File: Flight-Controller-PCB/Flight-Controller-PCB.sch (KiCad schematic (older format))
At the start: 24 parts, among them J1 Power_In, J2 ESC_1, J3 ESC_2, J4 ESC_3, J5 ESC_4, J6 Receiver, J7 Aux, U1 MCP6001U

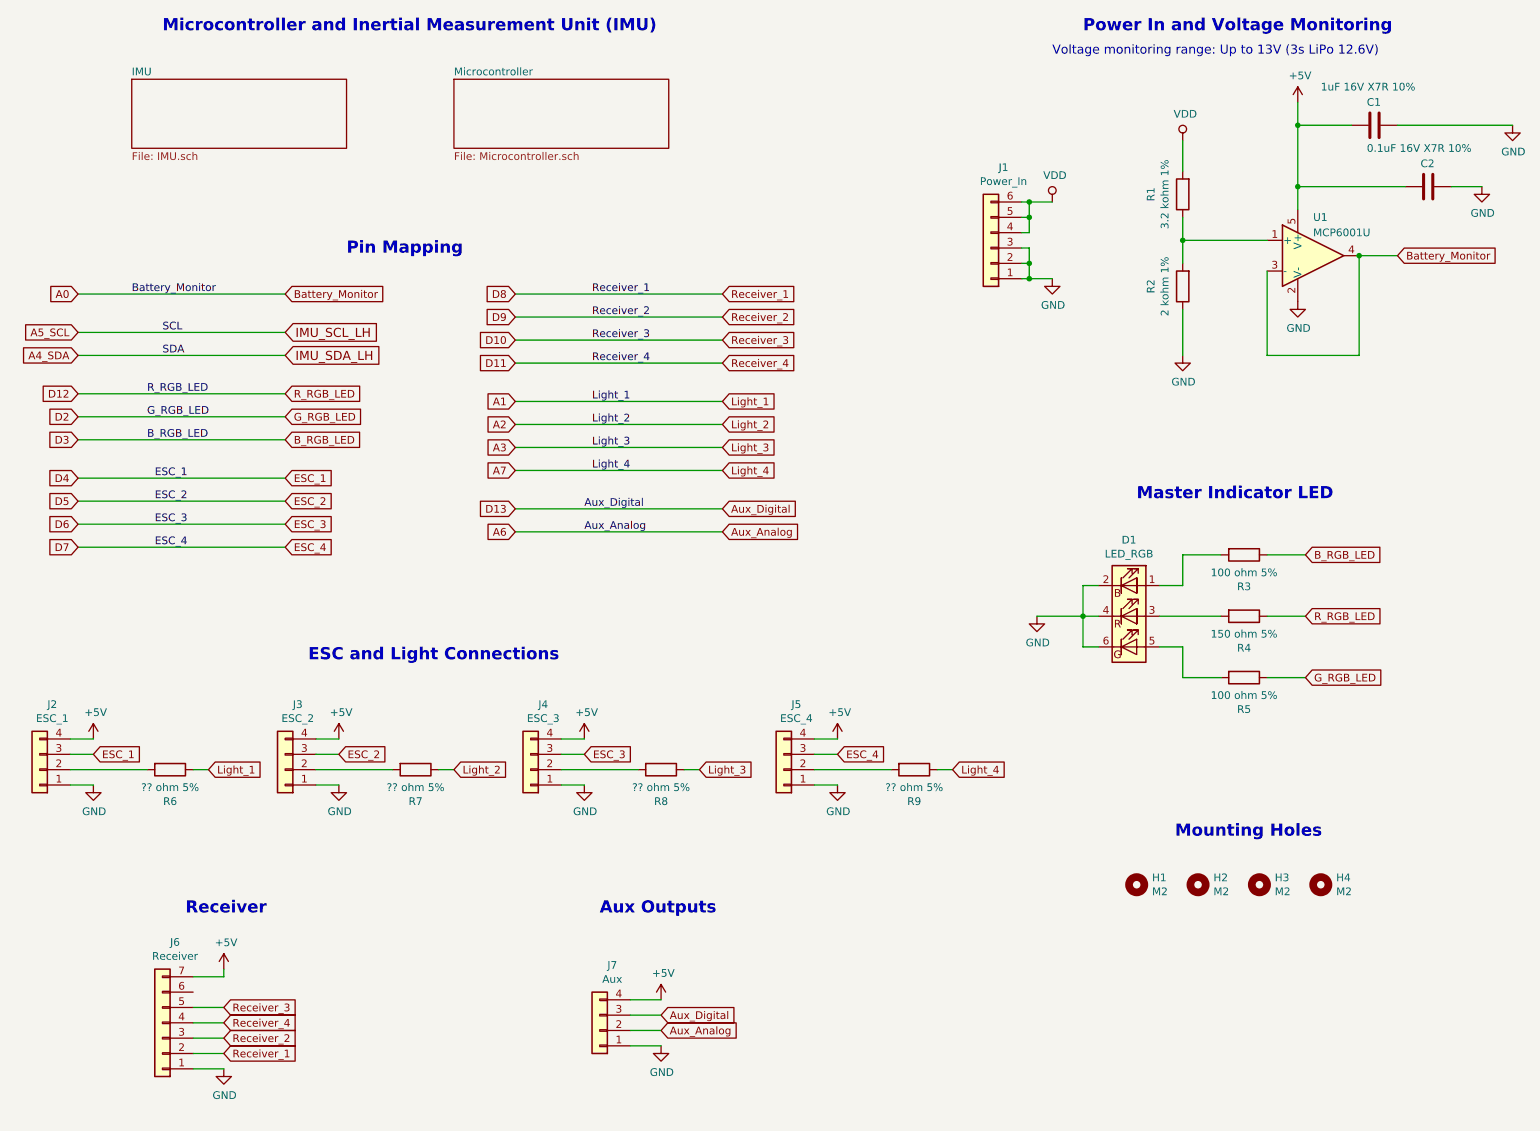
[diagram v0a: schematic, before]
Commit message: Deleted majority of unused components. Started schematic for new MCU
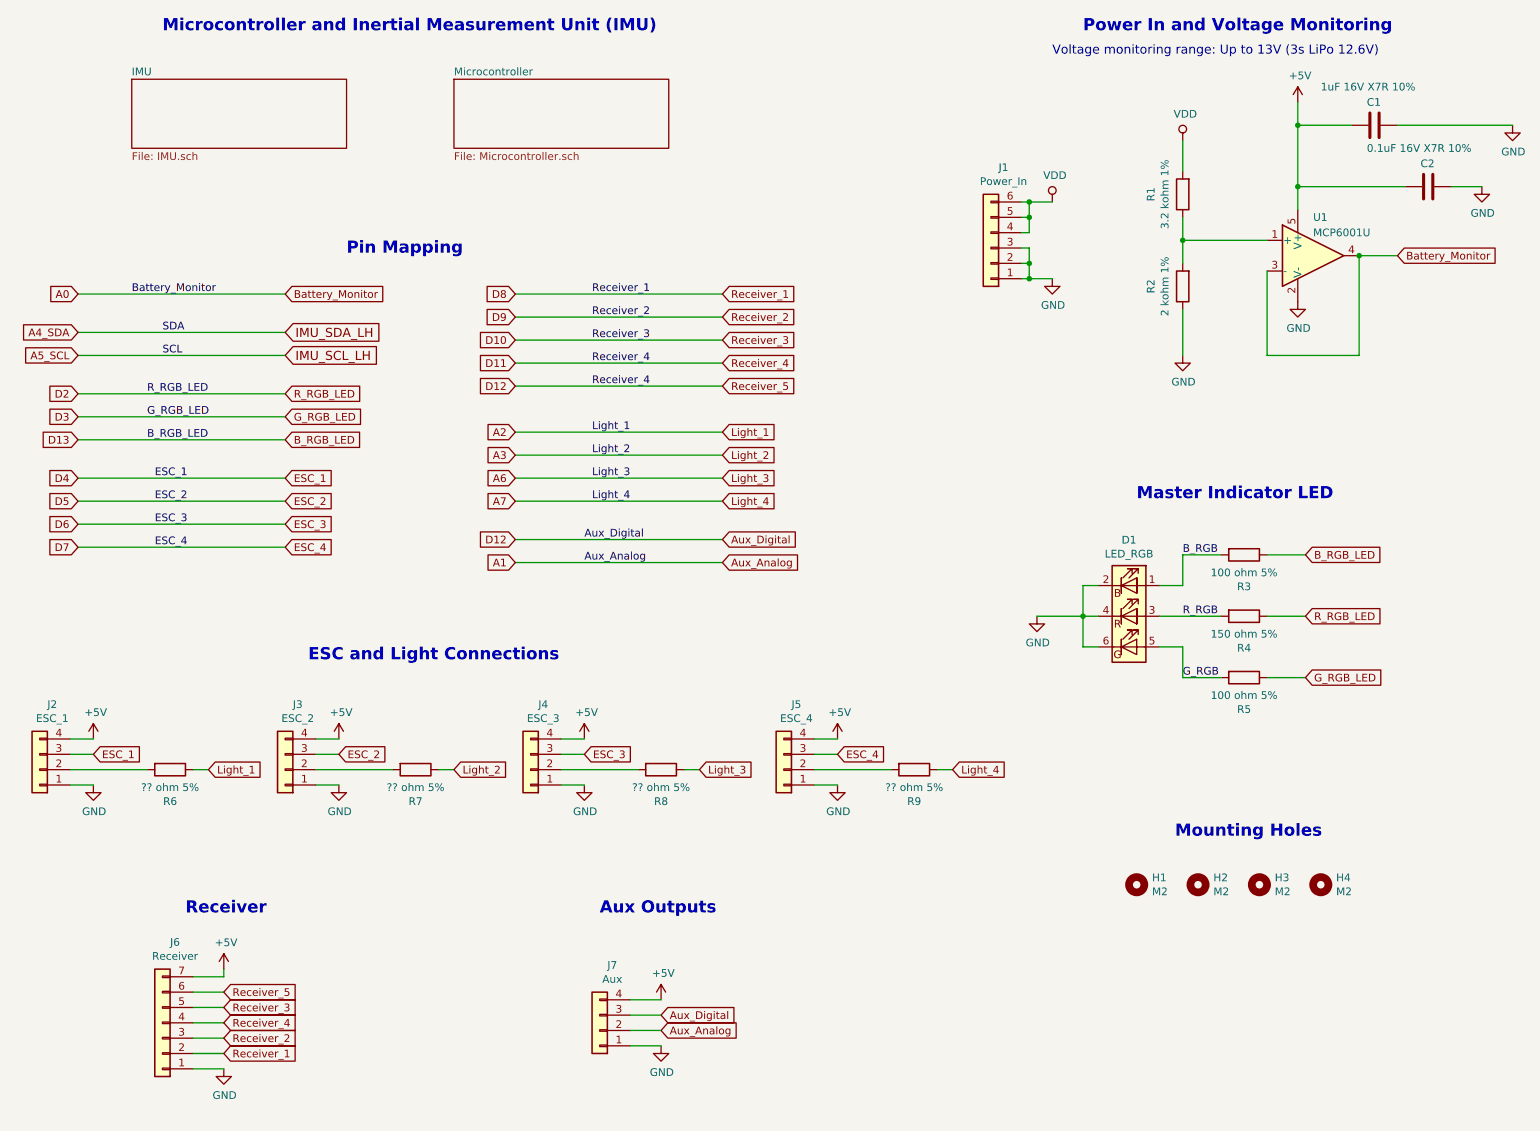
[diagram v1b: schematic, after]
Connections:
- net D11 is gone; now on net Aux_Digital: J6.4 (Pin_4)
- net D12 is gone; now on net D2: R4.1
- net A1: now also J7.2 (Pin_2); no longer R6.1
- net A2: now also R6.1; no longer R7.1
- net A3: now also R7.1; no longer R8.1
- net A6: now also R8.1; no longer J7.2 (Pin_2)
- net Aux_Digital: now also J6.6 (Pin_6)
- net D2: no longer R5.1
- net B_RGB: now reaches D1.1 (RA), R3.2
- net R_RGB: now reaches D1.3 (GA), R4.2
- net G_RGB: now reaches D1.5 (BA), R5.2
- new net D3: R5.1
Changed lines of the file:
@@
 EESchema Schematic File Version 4
-LIBS:Main-Board-cache
 EELAYER 30 0
 EELAYER END
@@
 	9350 2200 9600 2200
 Connection ~ 9350 2200
+Text GLabel 2350 2850 2    59   Input ~ 0
+IMU_SCL_LH
 Text GLabel 2350 2700 2    59   Input ~ 0
-IMU_SCL_LH
-Text GLabel 2350 2850 2    59   Input ~ 0
 IMU_SDA_LH
+Text GLabel 1000 2850 0    50   Input ~ 0
+A5_SCL
 Text GLabel 1000 2700 0    50   Input ~ 0
-A5_SCL
-Text GLabel 1000 2850 0    50   Input ~ 0
 A4_SDA
 Text Notes 7900 3800 0    79   ~ 16
@@
 	5200 2900 3850 2900
 Text GLabel 1000 3250 0    50   Input ~ 0
-D2
+D3
 Wire Wire Line
 	1000 3100 2350 3100
@@
 	2350 3400 1000 3400
 Wire Wire Line
+	1000 2850 2350 2850
+Wire Wire Line
 	1000 2700 2350 2700
 Wire Wire Line
-	1000 2850 2350 2850
-Wire Wire Line
 	1000 2450 2350 2450
-Text GLabel 5200 3150 2    50   Input ~ 0
+Text GLabel 5200 3350 2    50   Input ~ 0
 Light_1
-Text GLabel 5200 3300 2    50   Input ~ 0
+Text GLabel 5200 3500 2    50   Input ~ 0
 Light_2
-Text GLabel 5200 3450 2    50   Input ~ 0
+Text GLabel 5200 3650 2    50   Input ~ 0
 Light_3
-Text GLabel 5200 3600 2    50   Input ~ 0
+Text GLabel 5200 3800 2    50   Input ~ 0
 Light_4
-Text GLabel 3850 3150 0    50   Input ~ 0
-A1
-Text GLabel 3850 3300 0    50   Input ~ 0
+Text GLabel 3850 3350 0    50   Input ~ 0
 A2
-Text GLabel 3850 3450 0    50   Input ~ 0
+Text GLabel 3850 3500 0    50   Input ~ 0
 A3
-Text GLabel 3850 3600 0    50   Input ~ 0
+Text GLabel 3850 3650 0    50   Input ~ 0
+A6
+Text GLabel 3850 3800 0    50   Input ~ 0
 A7
 Wire Wire Line
-	3850 3150 5200 3150
-Wire Wire Line
-	5200 3300 3850 3300
-Wire Wire Line
-	3850 3450 5200 3450
-Wire Wire Line
-	5200 3600 3850 3600
+	3850 3350 5200 3350
+Wire Wire Line
+	5200 3500 3850 3500
+Wire Wire Line
+	3850 3650 5200 3650
+Wire Wire Line
+	5200 3800 3850 3800
 Text GLabel 1850 5550 2    50   Input ~ 0
 Light_1
@@
 Text Label 1350 2450 0    50   ~ 0
 Battery_Monitor
+Text Label 1550 2850 0    50   ~ 0
+SCL
 Text Label 1550 2700 0    50   ~ 0
-SCL
-Text Label 1550 2850 0    50   ~ 0
 SDA
 Text Label 1450 3100 0    50   ~ 0
@@
 $EndComp
 Text GLabel 1000 3100 0    50   Input ~ 0
-D12
+D2
 Text GLabel 1000 3400 0    50   Input ~ 0
-D3
+D13
 Text Label 4350 2450 0    50   ~ 0
 Receiver_1
@@
 Text Label 4350 2900 0    50   ~ 0
 Receiver_4
-Text Label 4350 3150 0    50   ~ 0
+Text Label 4350 3350 0    50   ~ 0
 Light_1
-Text Label 4350 3300 0    50   ~ 0
+Text Label 4350 3500 0    50   ~ 0
 Light_2
-Text Label 4350 3450 0    50   ~ 0
+Text Label 4350 3650 0    50   ~ 0
 Light_3
-Text Label 4350 3600 0    50   ~ 0
+Text Label 4350 3800 0    50   ~ 0
 Light_4
 Wire Wire Line
@@
 Text Notes 4400 6500 0    79   ~ 16
 Aux Outputs
-Text GLabel 3850 3850 0    50   Input ~ 0
-D13
-Text GLabel 3850 4000 0    50   Input ~ 0
-A6
-Text GLabel 5200 3850 2    50   Input ~ 0
+Text GLabel 3850 4050 0    50   Input ~ 0
+D12
+Text GLabel 3850 4200 0    50   Input ~ 0
+A1
+Text GLabel 5200 4050 2    50   Input ~ 0
 Aux_Digital
-Text GLabel 5200 4000 2    50   Input ~ 0
+Text GLabel 5200 4200 2    50   Input ~ 0
 Aux_Analog
 Wire Wire Line
-	3850 3850 5200 3850
-Wire Wire Line
-	5200 4000 3850 4000
-Text Label 4300 3850 0    50   ~ 0
+	3850 4050 5200 4050
+Wire Wire Line
+	5200 4200 3850 4200
+Text Label 4300 4050 0    50   ~ 0
 Aux_Digital
-Text Label 4300 4000 0    50   ~ 0
+Text Label 4300 4200 0    50   ~ 0
 Aux_Analog
 Text GLabel 4800 7150 2    50   Input ~ 0
@@
 Wire Wire Line
 	8750 4550 9000 4550
+Text GLabel 5200 3050 2    50   Input ~ 0
+Receiver_5
+Text GLabel 3850 3050 0    50   Input ~ 0
+D12
+Wire Wire Line
+	5200 3050 3850 3050
+Text Label 4350 3050 0    50   ~ 0
+Receiver_4
+Text GLabel 1950 7000 2    50   Input ~ 0
+Receiver_5
+Wire Wire Line
+	1750 7000 1950 7000
+Text Label 8200 4150 0    50   ~ 0
+B_RGB
+Text Label 8200 4550 0    50   ~ 0
+R_RGB
+Text Label 8200 4950 0    50   ~ 0
+G_RGB
 $EndSCHEMATC

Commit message: Push before branch switch
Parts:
- added D? (x2): LED, LED_SMD:LED_0603_1608Metric_Pad1.05x0.95mm_HandSolder, symbol Device:LED
- added R? (x2): ?? ohm 5%, Resistor_SMD:R_0603_1608Metric_Pad1.05x0.95mm_HandSolder, symbol Device:R
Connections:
- net +5V: now also R?.1
- net GND: now also D?.1 (K), D?.1 (K)
- new net: D?.2 (A), R?.2 (x2)
- new net +3V3: R?.1
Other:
- note added: "Master Indicator LEDs"
- note removed: "Master Indicator LED"
- moved on the sheet: D1, H1, H2, H3, H4, R3, R4, R5
